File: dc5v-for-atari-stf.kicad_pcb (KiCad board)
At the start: 2 copper layers, 135 x 90 mm, 15 parts, among them J1 Conn_01x03, J2 Conn_01x06, J3 Adjustable MT3608 module, J4 Fixed 12V module, J5 Conn_01x02, SW1 Momentary or Latched

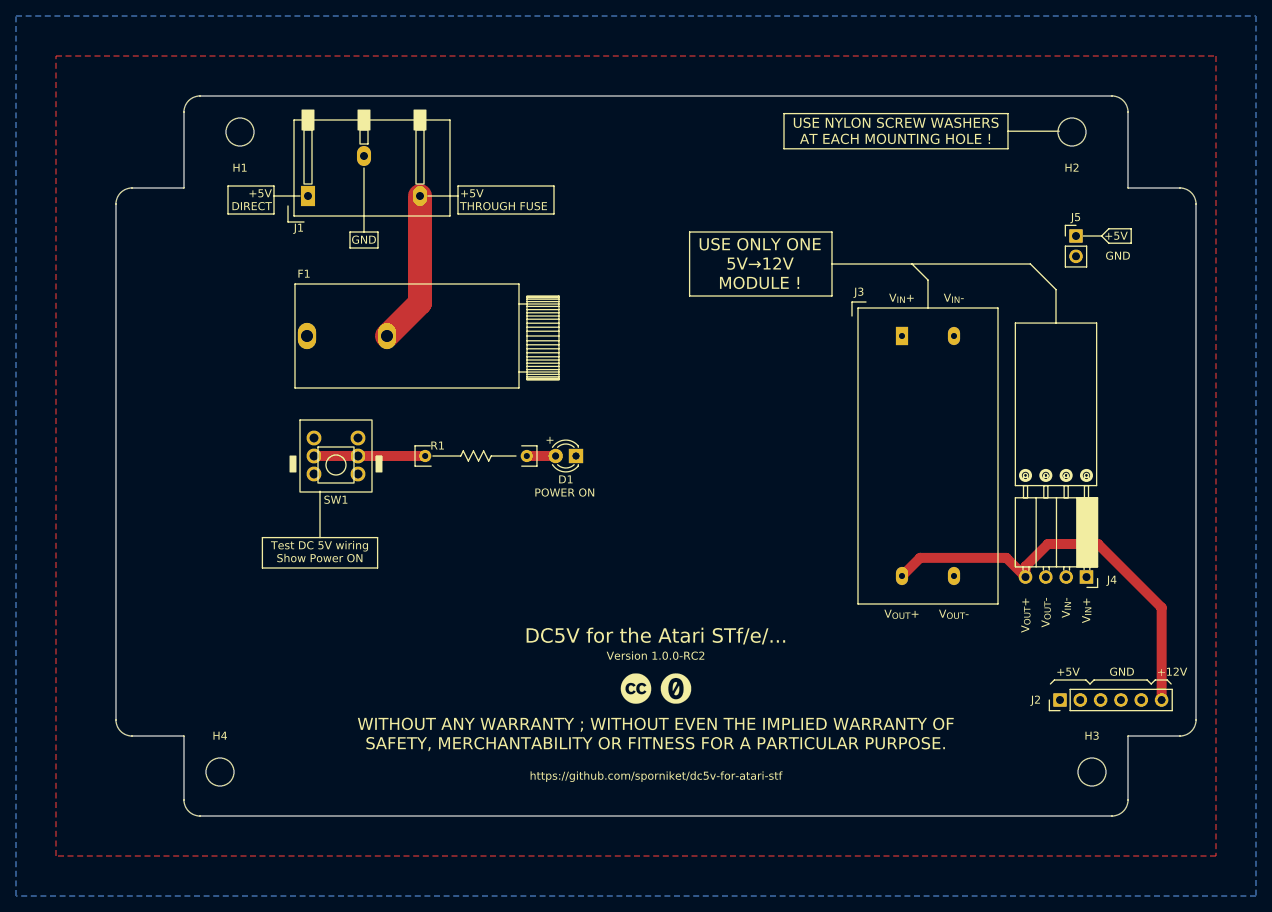
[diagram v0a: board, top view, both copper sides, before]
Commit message: Various fixes toward final releases : block terminal footprint and positionning, labels
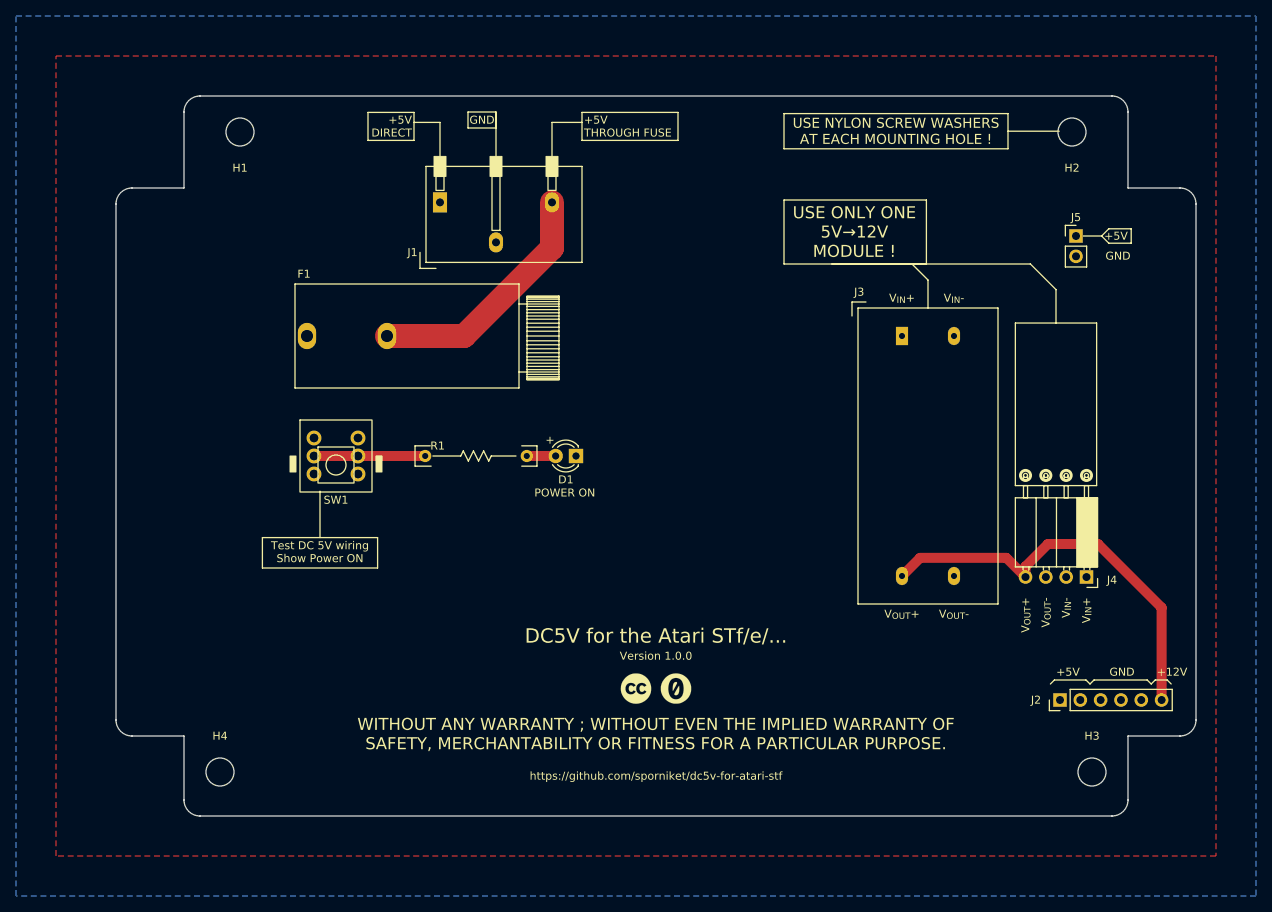
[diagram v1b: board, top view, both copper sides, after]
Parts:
- moved J1 17.5 mm to (130.0, 70.8)
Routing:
- net Net-(F1-Pad2): track 19.2 -> 30.9 mm
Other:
- board text added: "Version 1.0.0"
- board text removed: "Version 1.0.0-RC2"

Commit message: finalise v1.0.0
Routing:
- net +12V: track 51.7 -> 44.7 mm
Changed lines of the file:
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@@
   (title_block
     (title "DC5V for the Atari STf/e/...")
-    (date "2023-10-15")
+    (date "2023-10-31")
     (rev "v1.0.0")
     (company "Sporniket")
@@
         (effects (font (size 1 1) (thickness 0.15)))
     )
-    (fp_text user "V_{IN}+" (at 3.81 2.54 90 unlocked) (layer "F.SilkS")
+    (fp_text user "V_{OUT}-" (at 1.295 2.54 90 unlocked) (layer "F.SilkS")
         (effects (font (size 1 1) (thickness 0.15)) (justify right))
     )
-    (fp_text user "V_{OUT}+" (at -3.81 2.54 90 unlocked) (layer "F.SilkS")
+    (fp_text user "V_{OUT}+" (at 3.835 2.54 90 unlocked) (layer "F.SilkS")
         (effects (font (size 1 1) (thickness 0.15)) (justify right))
     )
-    (fp_text user "V_{IN}-" (at 1.27 2.54 90 unlocked) (layer "F.SilkS")
+    (fp_text user "V_{IN}+" (at -3.785 2.54 90 unlocked) (layer "F.SilkS")
         (effects (font (size 1 1) (thickness 0.15)) (justify right))
     )
-    (fp_text user "V_{OUT}-" (at -1.27 2.54 90 unlocked) (layer "F.SilkS")
+    (fp_text user "V_{IN}-" (at -1.245 2.54 90 unlocked) (layer "F.SilkS")
         (effects (font (size 1 1) (thickness 0.15)) (justify right))
     )
@@
         (effects (font (size 1 1) (thickness 0.15)))
     )
+    (fp_line (start -5.588 -10.414) (end -5.08 -10.414)
+      (stroke (width 0.12) (type default)) (layer "F.SilkS"))
+    (fp_line (start -5.588 -0.762) (end -5.588 -10.414)
+      (stroke (width 0.12) (type default)) (layer "F.SilkS"))
     (fp_line (start -5.08 -31.75) (end -5.08 -11.43)
       (stroke (width 0.12) (type solid)) (layer "F.SilkS"))
@@
     (fp_line (start -5.08 -9.903) (end -5.08 -1.273)
       (stroke (width 0.12) (type solid)) (layer "F.SilkS"))
+    (fp_line (start -5.08 -0.762) (end -5.588 -0.762)
+      (stroke (width 0.12) (type default)) (layer "F.SilkS"))
+    (fp_line (start -5.08 -0.762) (end -5.08 1.27)
+      (stroke (width 0.12) (type default)) (layer "F.SilkS"))
+    (fp_line (start -5.08 1.27) (end -3.81 1.27)
+      (stroke (width 0.12) (type default)) (layer "F.SilkS"))
     (fp_line (start -4.11 -1.273) (end -4.11 -0.863)
       (stroke (width 0.12) (type solid)) (layer "F.SilkS"))
@@
     (fp_line (start 2.6 -9.903) (end 2.6 -1.273)
       (stroke (width 0.12) (type solid)) (layer "F.SilkS"))
-    (fp_line (start 2.7181 -9.903) (end 2.7181 -1.273)
-      (stroke (width 0.12) (type solid)) (layer "F.SilkS"))
-    (fp_line (start 2.836195 -9.903) (end 2.836195 -1.273)
-      (stroke (width 0.12) (type solid)) (layer "F.SilkS"))
-    (fp_line (start 2.95429 -9.903) (end 2.95429 -1.273)
-      (stroke (width 0.12) (type solid)) (layer "F.SilkS"))
-    (fp_line (start 3.072385 -9.903) (end 3.072385 -1.273)
-      (stroke (width 0.12) (type solid)) (layer "F.SilkS"))
-    (fp_line (start 3.19048 -9.903) (end 3.19048 -1.273)
-      (stroke (width 0.12) (type solid)) (layer "F.SilkS"))
-    (fp_line (start 3.308575 -9.903) (end 3.308575 -1.273)
-      (stroke (width 0.12) (type solid)) (layer "F.SilkS"))
-    (fp_line (start 3.42667 -9.903) (end 3.42667 -1.273)
-      (stroke (width 0.12) (type solid)) (layer "F.SilkS"))
     (fp_line (start 3.51 -1.273) (end 3.51 -0.923)
       (stroke (width 0.12) (type solid)) (layer "F.SilkS"))
-    (fp_line (start 3.544765 -9.903) (end 3.544765 -1.273)
-      (stroke (width 0.12) (type solid)) (layer "F.SilkS"))
     (fp_line (start 3.556 -12.192) (end 3.556 -12.7)
       (stroke (width 0.12) (type solid)) (layer "F.SilkS"))
-    (fp_line (start 3.66286 -9.903) (end 3.66286 -1.273)
-      (stroke (width 0.12) (type solid)) (layer "F.SilkS"))
-    (fp_line (start 3.780955 -9.903) (end 3.780955 -1.273)
-      (stroke (width 0.12) (type solid)) (layer "F.SilkS"))
-    (fp_line (start 3.89905 -9.903) (end 3.89905 -1.273)
-      (stroke (width 0.12) (type solid)) (layer "F.SilkS"))
-    (fp_line (start 4.017145 -9.903) (end 4.017145 -1.273)
-      (stroke (width 0.12) (type solid)) (layer "F.SilkS"))
     (fp_line (start 4.064 -12.192) (end 4.064 -12.7)
       (stroke (width 0.12) (type solid)) (layer "F.SilkS"))
-    (fp_line (start 4.13524 -9.903) (end 4.13524 -1.273)
-      (stroke (width 0.12) (type solid)) (layer "F.SilkS"))
     (fp_line (start 4.23 -1.273) (end 4.23 -0.923)
       (stroke (width 0.12) (type solid)) (layer "F.SilkS"))
-    (fp_line (start 4.253335 -9.903) (end 4.253335 -1.273)
-      (stroke (width 0.12) (type solid)) (layer "F.SilkS"))
-    (fp_line (start 4.37143 -9.903) (end 4.37143 -1.273)
-      (stroke (width 0.12) (type solid)) (layer "F.SilkS"))
-    (fp_line (start 4.489525 -9.903) (end 4.489525 -1.273)
-      (stroke (width 0.12) (type solid)) (layer "F.SilkS"))
-    (fp_line (start 4.60762 -9.903) (end 4.60762 -1.273)
-      (stroke (width 0.12) (type solid)) (layer "F.SilkS"))
-    (fp_line (start 4.725715 -9.903) (end 4.725715 -1.273)
-      (stroke (width 0.12) (type solid)) (layer "F.SilkS"))
-    (fp_line (start 4.84381 -9.903) (end 4.84381 -1.273)
-      (stroke (width 0.12) (type solid)) (layer "F.SilkS"))
-    (fp_line (start 4.961905 -9.903) (end 4.961905 -1.273)
-      (stroke (width 0.12) (type solid)) (layer "F.SilkS"))
     (fp_line (start 5.08 -31.75) (end -5.08 -31.75)
       (stroke (width 0.12) (type solid)) (layer "F.SilkS"))
     (fp_line (start 5.08 -11.43) (end 5.08 -31.75)
       (stroke (width 0.12) (type solid)) (layer "F.SilkS"))
-    (fp_line (start 5.08 -9.903) (end 5.08 -1.273)
-      (stroke (width 0.12) (type solid)) (layer "F.SilkS"))
     (fp_line (start 5.2 -9.903) (end -5.08 -9.903)
       (stroke (width 0.12) (type solid)) (layer "F.SilkS"))
@@
     (fp_line (start 5.2 -1.273) (end -5.08 -1.273)
       (stroke (width 0.12) (type solid)) (layer "F.SilkS"))
-    (fp_line (start 5.2 0.187) (end 5.2 1.297)
-      (stroke (width 0.12) (type solid)) (layer "F.SilkS"))
-    (fp_line (start 5.2 1.297) (end 3.87 1.297)
-      (stroke (width 0.12) (type solid)) (layer "F.SilkS"))
+    (fp_rect (start -5.08 -9.903) (end -2.48 -1.273)
+      (stroke (width 0.12) (type solid)) (fill solid) (layer "F.SilkS"))
     (fp_rect (start -4.064 -11.43) (end -3.556 -9.906)
       (stroke (width 0.12) (type solid)) (fill none) (layer "F.SilkS"))
@@
     (fp_line (start 5.08 -2.369) (end 4.11 -1.399)
       (stroke (width 0.1) (type solid)) (layer "F.Fab"))
-    (pad "1" thru_hole rect (at 3.81 0 270) (size 1.7 1.7) (drill 1) (layers "*.Cu" "*.Mask")
+    (pad "1" thru_hole rect (at -3.81 0 270) (size 1.7 1.7) (drill 1) (layers "*.Cu" "*.Mask")
       (net 3 "+5V") (pinfunction "Pin_1") (pintype "passive"))
-    (pad "2" thru_hole oval (at 1.27 0 270) (size 1.7 1.7) (drill 1) (layers "*.Cu" "*.Mask")
+    (pad "2" thru_hole oval (at -1.27 0 270) (size 1.7 1.7) (drill 1) (layers "*.Cu" "*.Mask")
       (net 1 "GND") (pinfunction "Pin_2") (pintype "passive"))
-    (pad "3" thru_hole oval (at -1.27 0 270) (size 1.7 1.7) (drill 1) (layers "*.Cu" "*.Mask")
+    (pad "3" thru_hole oval (at 1.27 0 270) (size 1.7 1.7) (drill 1) (layers "*.Cu" "*.Mask")
       (net 1 "GND") (pinfunction "Pin_3") (pintype "passive"))
-    (pad "4" thru_hole oval (at -3.81 0 270) (size 1.7 1.7) (drill 1) (layers "*.Cu" "*.Mask")
+    (pad "4" thru_hole oval (at 3.81 0 270) (size 1.7 1.7) (drill 1) (layers "*.Cu" "*.Mask")
       (net 4 "+12V") (pinfunction "Pin_4") (pintype "passive"))
     (model "${KICAD6_3DMODEL_DIR}/Connector_PinSocket_2.54mm.3dshapes/PinSocket_1x04_P2.54mm_Horizontal.wrl"
-      (offset (xyz 3.75 0 0))
+      (offset (xyz 3.81 0 0))
       (scale (xyz 1 1 1))
       (rotate (xyz 0 0 90))
@@
   )
   (segment (start 133.85 100) (end 137.46 100) (width 1.25) (layer "F.Cu") (net 2))
-  (segment (start 199 111) (end 196.19 113.81) (width 1.25) (layer "F.Cu") (net 4))
-  (segment (start 196.19 113.81) (end 196.19 115.13) (width 1.25) (layer "F.Cu") (net 4))
-  (segment (start 213.2 118.95) (end 205.25 111) (width 1.25) (layer "F.Cu") (net 4))
-  (segment (start 193.79248 112.73248) (end 196.19 115.13) (width 1.25) (layer "F.Cu") (net 4))
+  (segment (start 213.2 124.52) (end 213.2 130.5) (width 1.25) (layer "F.Cu") (net 4))
+  (segment (start 203.81 114.284656) (end 203.81 115.13) (width 1.25) (layer "F.Cu") (net 4))
+  (segment (start 202.257824 112.73248) (end 203.81 114.284656) (width 1.25) (layer "F.Cu") (net 4))
+  (segment (start 193.79248 112.73248) (end 202.257824 112.73248) (width 1.25) (layer "F.Cu") (net 4))
+  (segment (start 203.81 115.13) (end 213.2 124.52) (width 1.25) (layer "F.Cu") (net 4))
   (segment (start 183.017519 112.73248) (end 193.79248 112.73248) (width 1.25) (layer "F.Cu") (net 4))
   (segment (start 180.749999 115) (end 183.017519 112.73248) (width 1.25) (layer "F.Cu") (net 4))
-  (segment (start 213.2 130.5) (end 213.2 118.95) (width 1.25) (layer "F.Cu") (net 4))
-  (segment (start 205.25 111) (end 199 111) (width 1.25) (layer "F.Cu") (net 4))
   (segment (start 107.25 100) (end 112.75 100) (width 1.25) (layer "F.Cu") (net 5))
   (segment (start 112.75 100) (end 121.15 100) (width 1.25) (layer "F.Cu") (net 5))
